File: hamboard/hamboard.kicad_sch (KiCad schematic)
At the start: 38 parts, among them J1 Conn_01x03_Male, J2 Conn_01x24_Male, J3 USB_B_Micro, J4 Screw_Terminal_Btn, J5 Screw_Terminal_01x02, J6 programmer, Q1 AO3400A, Q2 S8050, Q3 S8050, U1 PCA9557PW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

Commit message: board: bom
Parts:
- removed J1: Conn_01x03_Male, Connector_PinHeader_2.54mm:PinHeader_1x03_P2.54mm_Vertical, symbol Connector:Conn_01x03_Male
- removed Q2, Q3: S8050, Package_TO_SOT_THT:TO-92_Inline, symbol Transistor_BJT:S8050
- removed TP1, TP2, TP3: TestPoint, TestPoint:TestPoint_Pad_D1.5mm, symbol Connector:TestPoint
- added C34: 15pF, Capacitor_SMD:C_0805_2012Metric, symbol Device:C
- added J1: i2c, TerminalBlock:TerminalBlock_bornier-4_P5.08mm, symbol Connector:Screw_Terminal_01x04
- added J10: Conn_01x03_Male, Connector_PinHeader_2.54mm:PinHeader_1x03_P2.54mm_Vertical, symbol Connector:Conn_01x03_Male
- added Q2, Q3: S8050, Package_TO_SOT_SMD:SOT-23, symbol Device:Q_NPN_BEC
- added R6: 1k, Resistor_SMD:R_0805_2012Metric, symbol Device:R
- added TP10, TP11: TestPoint, TestPoint:TestPoint_Pad_D1.5mm, symbol Connector:TestPoint
- C1: LCSC (none) -> C282732
- C2: LCSC (none) -> C29277
- C24, C4, C6: value C -> 1uF; LCSC (none) -> C2798196
- C26, C7: value C -> 100nF; LCSC (none) -> C282732
- C27, C8: value C -> 10nF; LCSC (none) -> C376921
- C3: value 0.1uF -> 100nF; LCSC (none) -> C282732
- C5: value ? -> 100nF; LCSC (none) -> C282732
- D1, D2: footprint Diode_SMD:D_SOD-923 -> hamboard:Diodes_DFN1006; LCSC (none) -> C2985641
- J2: footprint (none) -> Connector_FFC-FPC:Hirose_FH12-24S-0.5SH_1x24-1MP_P0.50mm_Horizontal; LCSC (none) -> C2858298
- J3: footprint Connector_USB:USB_Micro-B_Molex-105017-0001 -> Connector_USB:USB_Micro-B_GCT_USB3076-30-A; LCSC (none) -> C132562
- J4, J5: footprint Connector_Phoenix_MSTB:PhoenixContact_MSTBA_2,5_2-G-5,08_1x02_P5.08mm_Horizontal -> TerminalBlock:TerminalBlock_bornier-2_P5.08mm; LCSC (none) -> C394556
- Q1: LCSC (none) -> C347475
- R1, R2, R9: value R -> 10k; LCSC (none) -> C2930231
- R10: LCSC (none) -> C2907288
- R11: value 0R -> 10k; LCSC (none) -> C2930231
- R12, R13, R4, R5, R8: LCSC (none) -> C2930231
- U1: LCSC (none) -> C141380
- U2: LCSC (none) -> C529589
- U3: footprint Package_SO:SOIC-16_3.9x9.9mm_P1.27mm -> Package_SO:SOP-16_3.9x9.9mm_P1.27mm; LCSC (none) -> C84681
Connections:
- net +3V3: now also J1.1 (Pin_1)
- net BTN: now also R6.1; no longer J4.1 (Pin_1)
- net CAM_PCLK: now also C34.1
- net EN: now also Q2.3 (C)
- net GND: now also C34.2, J1.4 (Pin_4)
- net I2C_SCL: now also J1.2 (Pin_2)
- net I2C_SDA: now also J1.3 (Pin_3)
- net IO0: now also Q3.3 (C)
- net at U1.13 (IO6): now also J10.2 (Pin_2)
- net at D2.2 (A2), J3.2 (D-), U3.6 (UD-): now also TP11.1
- net at U1.12 (IO5): now also J10.3 (Pin_3)
- net at U1.14 (IO7): now also J10.1 (Pin_1)
- net at D1.2 (A2), J3.3 (D+), U3.5 (UD+): now also TP10.1
- net at R12.1, U3.13 (~{DTR}): now also Q3.2 (E)
- net at R13.2: now also Q3.1 (B)
- net at R13.1, U3.14 (~{RTS}): now also Q2.2 (E)
- net at R12.2: now also Q2.1 (B)
- new net: J4.1 (Pin_1), R6.2
- no-connect marks 0 -> 10
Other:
- moved on the sheet: C24, C26, C27, C5, C6, C7, C8, J4, R1, R2, R9

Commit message: first pcb layout
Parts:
- J1: footprint TerminalBlock:TerminalBlock_bornier-4_P5.08mm -> Connector_PinHeader_2.54mm:PinHeader_1x04_P2.54mm_Vertical
- U2: footprint lib:XCVR_ESP32-WROVER-E-N4R8 -> XCVR_ESP32-WROVER-E-N4R8; symbol esp32:ESP32-WROVER-E-N4R8 -> hamboard:ESP32-WROVER-E-N4R8
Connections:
- net +24V: now also J5.2 (Pin_2); no longer J5.1 (Pin_1)
- net BTN: now also U2.36 (IO22); no longer U2.6 (IO34)
- net CAM_HREF: now also U2.14 (IO12); no longer U2.24 (IO2)
- net CAM_PCLK: now also U2.9 (IO33); no longer U2.36 (IO22)
- net CAM_PWN: now also U1.6 (IO0); no longer U1.7 (IO1)
- net CAM_RST: now also U1.7 (IO1); no longer U1.6 (IO0)
- net CAM_VSYNC: now also U2.16 (IO13); no longer U2.29 (IO5)
- net CAM_XCLK: now also U2.12 (IO27); no longer U2.30 (IO18)
- net CAM_Y2: now also U2.7 (IO35); no longer U2.10 (IO25)
- net CAM_Y3: now also U2.5 (SENSOR_VN); no longer U2.12 (IO27)
- net CAM_Y4: now also U2.4 (SENSOR_VP); no longer U2.8 (IO32)
- net CAM_Y5: now also U2.6 (IO34); no longer U2.11 (IO26)
- net CAM_Y6: now also U2.8 (IO32); no longer U2.5 (SENSOR_VN)
- net CAM_Y7: now also U2.10 (IO25); no longer U2.4 (SENSOR_VP)
- net CAM_Y8: now also U2.11 (IO26); no longer U2.7 (IO35)
- net CAM_Y9: now also U2.13 (IO14); no longer U2.23 (IO15)
- net GND: now also U2.39_1 (EXP), U2.39_2 (EXP), U2.39_3 (EXP), U2.39_4 (EXP), U2.39_5 (EXP), U2.39_6 (EXP), U2.39_7 (EXP), U2.39_8 (EXP), U2.39_9 (EXP)
- net I2C_SCL: now also U2.23 (IO15); no longer U2.16 (IO13)
- net I2C_SDA: now also U2.24 (IO2); no longer U2.13 (IO14)
- net STEPPER_CS: now also U2.33 (IO21); no longer U2.31 (IO19)
- net STEPPER_DIR: now also U1.14 (IO7); no longer U1.11 (IO4)
- net STEPPER_EN: now also U1.13 (IO6); no longer U1.10 (IO3)
- net STEPPER_SCK: now also U2.31 (IO19); no longer U2.14 (IO12)
- net STEPPER_SDI: now also U2.30 (IO18); no longer U2.26 (IO4)
- net STEPPER_SDO: now also U2.29 (IO5); no longer U2.9 (IO33)
- net STEPPER_STEP: now also U2.26 (IO4); no longer U2.33 (IO21)
- net at Q1.3 (D): now also J5.1 (Pin_1); no longer J5.2 (Pin_2)
- net at J10.3 (Pin_3): now also U1.10 (IO3); no longer U1.12 (IO5)
- net at J10.2 (Pin_2): now also U1.11 (IO4); no longer U1.13 (IO6)
- net at J10.1 (Pin_1): now also U1.12 (IO5); no longer U1.14 (IO7)
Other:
- moved on the sheet: J10

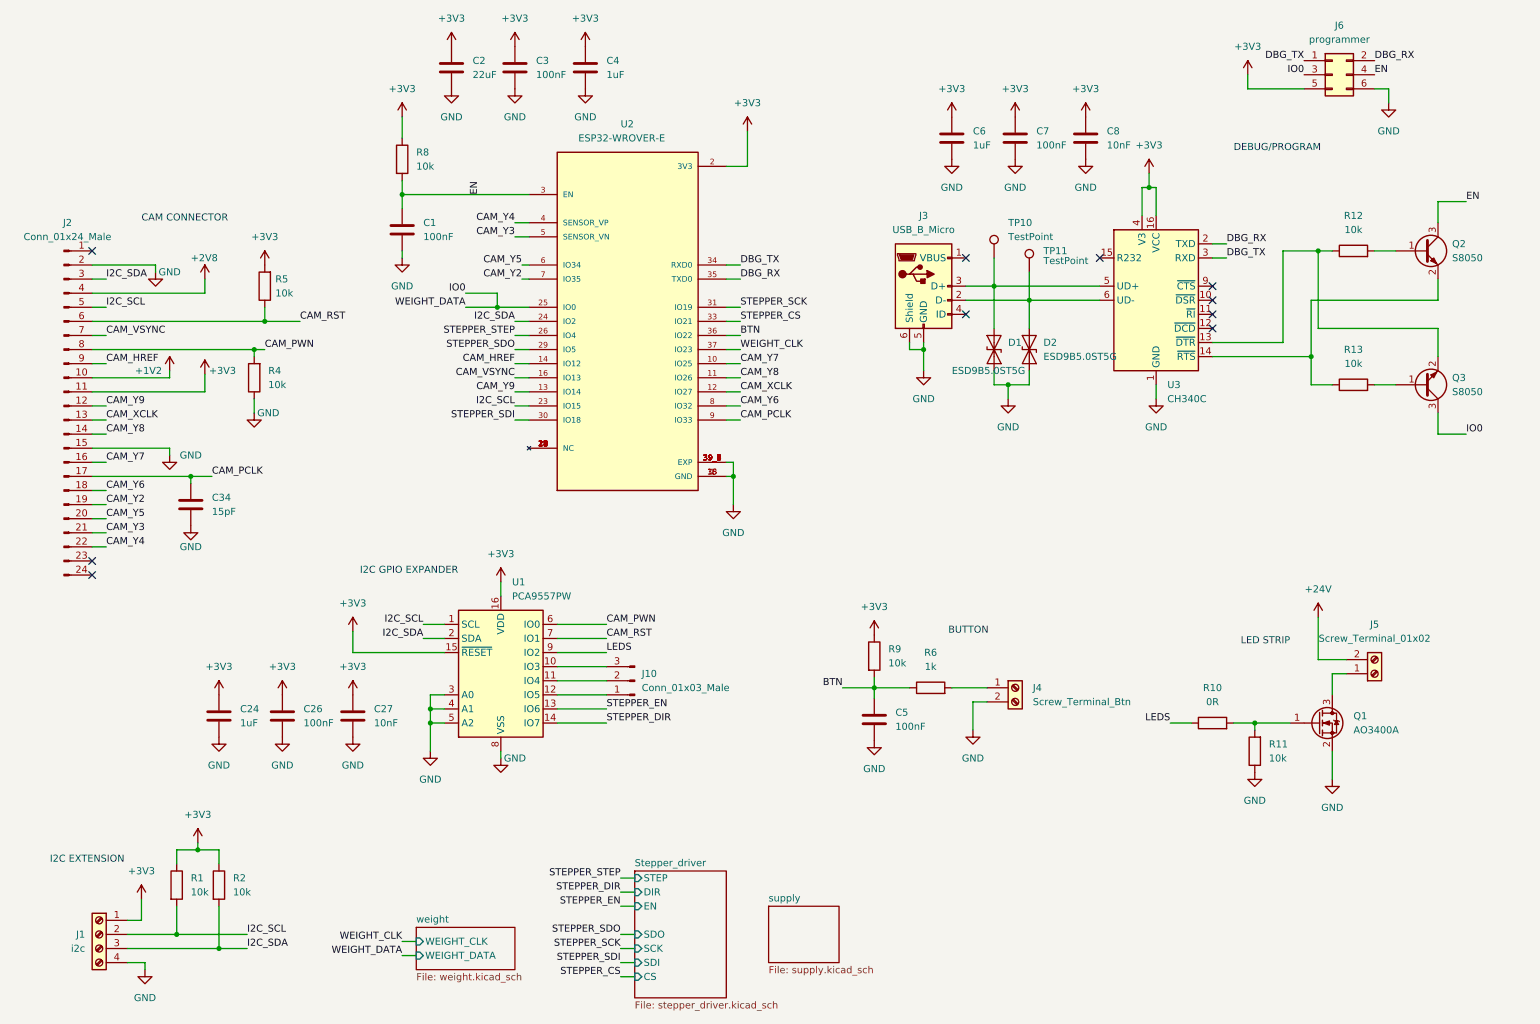
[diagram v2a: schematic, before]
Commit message: pcb: added screws and rerouted everything
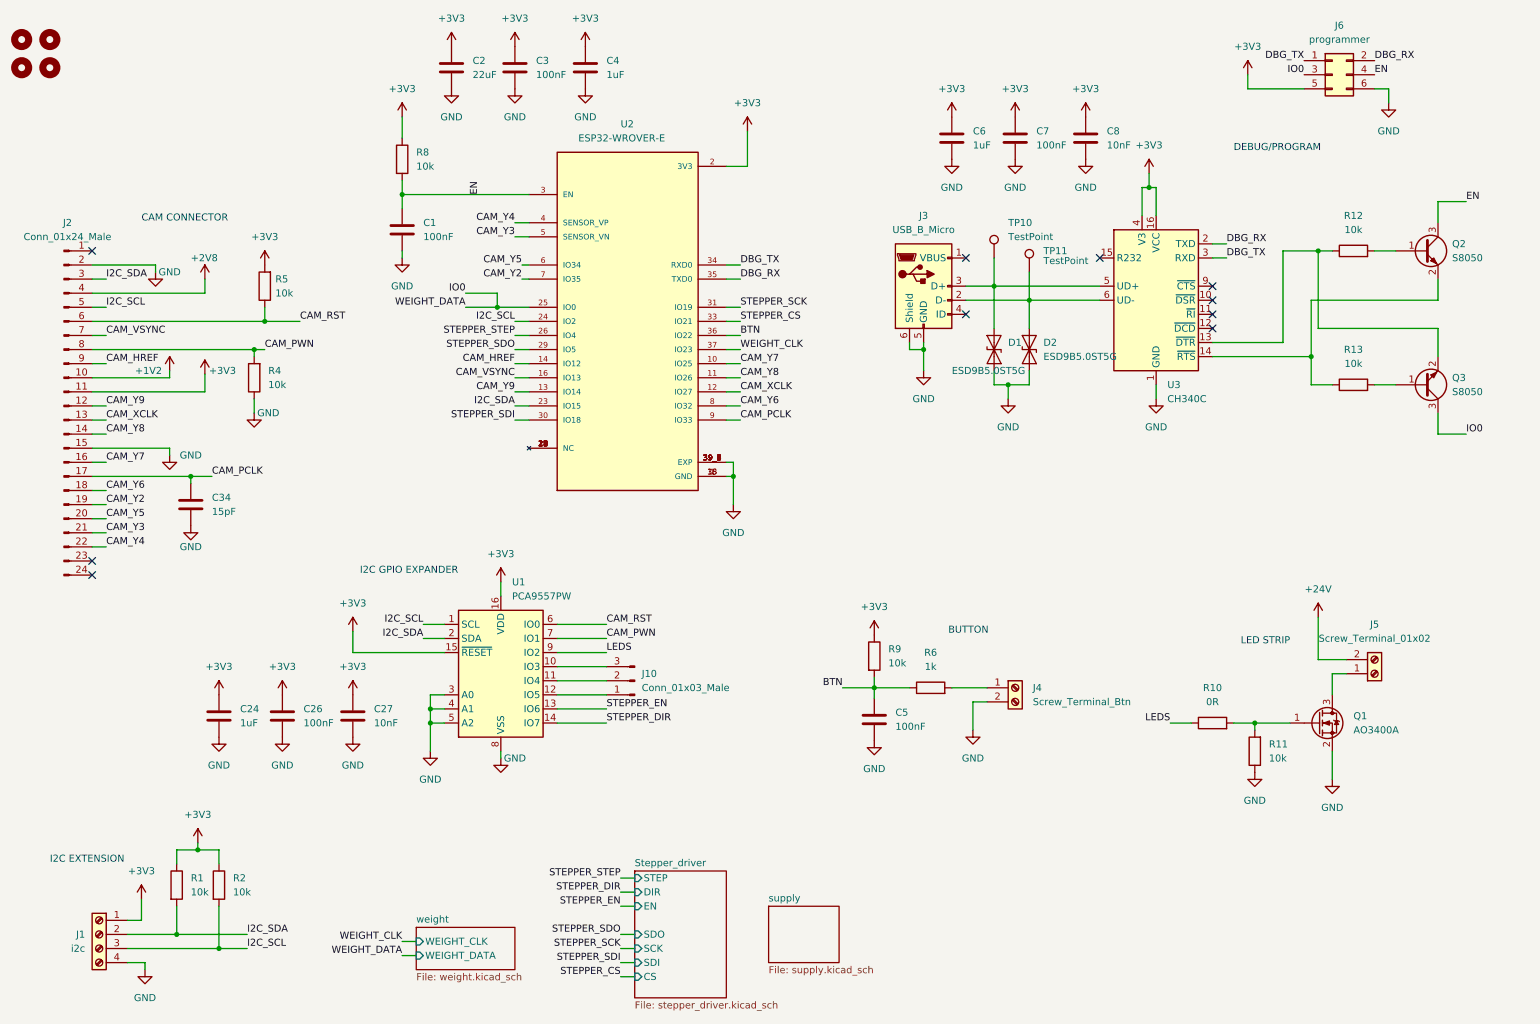
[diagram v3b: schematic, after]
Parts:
- added H1, H2, H3, H4: MountingHole, MountingHole:MountingHole_3.2mm_M3, symbol Mechanical:MountingHole
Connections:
- net CAM_PWN: now also U1.7 (IO1); no longer U1.6 (IO0)
- net CAM_RST: now also U1.6 (IO0); no longer U1.7 (IO1)
- net I2C_SCL: now also J1.3 (Pin_3), R2.2, U2.24 (IO2); no longer J1.2 (Pin_2), R1.2, U2.23 (IO15)
- net I2C_SDA: now also J1.2 (Pin_2), R1.2, U2.23 (IO15); no longer J1.3 (Pin_3), R2.2, U2.24 (IO2)
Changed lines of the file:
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@@
     (effects (font (size 1.27 1.27)) (justify left bottom))
   )
-  (label "I2C_SDA" (at 59.69 181.61 0)
+  (label "I2C_SDA" (at 59.69 179.07 0)
     (effects (font (size 1.27 1.27)) (justify left bottom))
   )
@@
     (effects (font (size 1.27 1.27)) (justify left bottom))
   )
-  (label "I2C_SCL" (at 59.69 179.07 0)
+  (label "I2C_SCL" (at 59.69 181.61 0)
     (effects (font (size 1.27 1.27)) (justify left bottom))
   )
@@
     (effects (font (size 1.27 1.27)) (justify right bottom))
   )
-  (label "I2C_SDA" (at 107.95 68.58 180)
+  (label "I2C_SDA" (at 107.95 83.82 180)
     (effects (font (size 1.27 1.27)) (justify right bottom))
   )
@@
     (effects (font (size 1.27 1.27)) (justify right bottom))
   )
-  (label "CAM_PWN" (at 124.46 123.19 0)
+  (label "CAM_PWN" (at 124.46 125.73 0)
     (effects (font (size 1.27 1.27)) (justify left bottom))
   )
@@
     (effects (font (size 1.27 1.27)) (justify right bottom))
   )
-  (label "I2C_SCL" (at 107.95 83.82 180)
+  (label "I2C_SCL" (at 107.95 68.58 180)
     (effects (font (size 1.27 1.27)) (justify right bottom))
   )
@@
     (effects (font (size 1.27 1.27)) (justify left bottom))
   )
-  (label "CAM_RST" (at 124.46 125.73 0)
+  (label "CAM_RST" (at 124.46 123.19 0)
     (effects (font (size 1.27 1.27)) (justify left bottom))
   )
@@
     (pin "4")
   )
+  (symbol (lib_id "Mechanical:MountingHole") (at 19.05 22.86 0) (unit 1)
+    (in_bom yes) (on_board yes) (fields_autoplaced)
+    (property "Reference" "H2" (id 0) (at 21.59 21.5899 0)
+      (effects (font (size 1.27 1.27)) (justify left) hide)
+    )
+    (property "Value" "MountingHole" (id 1) (at 21.59 24.1299 0)
+      (effects (font (size 1.27 1.27)) (justify left) hide)
+    )
+    (property "Footprint" "MountingHole:MountingHole_3.2mm_M3" (id 2) (at 19.05 22.86 0)
+      (effects (font (size 1.27 1.27)) hide)
+    )
+    (property "Datasheet" "~" (id 3) (at 19.05 22.86 0)
+      (effects (font (size 1.27 1.27)) hide)
+    )
+  )
   (symbol (lib_id "power:+1V2") (at 45.72 77.47 0) (unit 1)
     (in_bom yes) (on_board yes)
@@
     (pin "1")
     (pin "2")
+  )
+  (symbol (lib_id "Mechanical:MountingHole") (at 24.13 17.78 0) (unit 1)
+    (in_bom yes) (on_board yes) (fields_autoplaced)
+    (property "Reference" "H3" (id 0) (at 26.67 16.5099 0)
+      (effects (font (size 1.27 1.27)) (justify left) hide)
+    )
+    (property "Value" "MountingHole" (id 1) (at 26.67 19.0499 0)
+      (effects (font (size 1.27 1.27)) (justify left) hide)
+    )
+    (property "Footprint" "MountingHole:MountingHole_3.2mm_M3" (id 2) (at 24.13 17.78 0)
+      (effects (font (size 1.27 1.27)) hide)
+    )
+    (property "Datasheet" "~" (id 3) (at 24.13 17.78 0)
+      (effects (font (size 1.27 1.27)) hide)
+    )
   )
   (symbol (lib_id "power:+2V8") (at 52.07 60.96 0) (unit 1)
@@
     (pin "1")
     (pin "2")
+  )
+  (symbol (lib_id "Mechanical:MountingHole") (at 19.05 17.78 0) (unit 1)
+    (in_bom yes) (on_board yes) (fields_autoplaced)
+    (property "Reference" "H1" (id 0) (at 21.59 16.5099 0)
+      (effects (font (size 1.27 1.27)) (justify left) hide)
+    )
+    (property "Value" "MountingHole" (id 1) (at 21.59 19.0499 0)
+      (effects (font (size 1.27 1.27)) (justify left) hide)
+    )
+    (property "Footprint" "MountingHole:MountingHole_3.2mm_M3" (id 2) (at 19.05 17.78 0)
+      (effects (font (size 1.27 1.27)) hide)
+    )
+    (property "Datasheet" "~" (id 3) (at 19.05 17.78 0)
+      (effects (font (size 1.27 1.27)) hide)
+    )
   )
   (symbol (lib_id "power:+3V3") (at 50.8 162.56 0) (unit 1)
@@
     (pin "2")
   )
+  (symbol (lib_id "Mechanical:MountingHole") (at 24.13 22.86 0) (unit 1)
+    (in_bom yes) (on_board yes) (fields_autoplaced)
+    (property "Reference" "H4" (id 0) (at 26.67 21.5899 0)
+      (effects (font (size 1.27 1.27)) (justify left) hide)
+    )
+    (property "Value" "MountingHole" (id 1) (at 26.67 24.1299 0)
+      (effects (font (size 1.27 1.27)) (justify left) hide)
+    )
+    (property "Footprint" "MountingHole:MountingHole_3.2mm_M3" (id 2) (at 24.13 22.86 0)
+      (effects (font (size 1.27 1.27)) hide)
+    )
+    (property "Datasheet" "~" (id 3) (at 24.13 22.86 0)
+      (effects (font (size 1.27 1.27)) hide)
+    )
+  )
   (symbol (lib_id "power:GND") (at 78.74 143.51 0) (unit 1)
     (in_bom yes) (on_board yes) (fields_autoplaced)
@@
       (reference "F1") (unit 1) (value "Polyfuse 24V/4A") (footprint "Fuse:Fuse_2920_7451Metric")
     )
+    (path "/7152708c-a746-4345-8572-2a08cbce2cab"
+      (reference "H1") (unit 1) (value "MountingHole") (footprint "MountingHole:MountingHole_3.2mm_M3")
+    )
+    (path "/563ffce6-3179-445e-a692-66231995d1ac"
+      (reference "H2") (unit 1) (value "MountingHole") (footprint "MountingHole:MountingHole_3.2mm_M3")
+    )
+    (path "/5b5dd905-5cf3-4fc8-998a-66cd7dae92f7"
+      (reference "H3") (unit 1) (value "MountingHole") (footprint "MountingHole:MountingHole_3.2mm_M3")
+    )
+    (path "/9879b16b-7ddd-449f-b7b8-508ff38a3ef8"
+      (reference "H4") (unit 1) (value "MountingHole") (footprint "MountingHole:MountingHole_3.2mm_M3")
+    )
     (path "/55b84d23-2619-4bca-a5ce-c99f2a5d964e"
       (reference "J1") (unit 1) (value "i2c") (footprint "Connector_PinHeader_2.54mm:PinHeader_1x04_P2.54mm_Vertical")
@@
       (reference "TP7") (unit 1) (value "TestPoint") (footprint "TestPoint:TestPoint_Pad_D1.5mm")
     )
-    (path "/cf781b29-da03-4e54-8f16-c9e2324f91c7/d88693b6-6dfc-4dd3-877e-759e3c4b167a"
-      (reference "TP8") (unit 1) (value "TestPoint") (footprint "TestPoint:TestPoint_Pad_D1.5mm")
-    )
     (path "/cf781b29-da03-4e54-8f16-c9e2324f91c7/ec254d83-55bb-4786-a17e-eae3949daeeb"

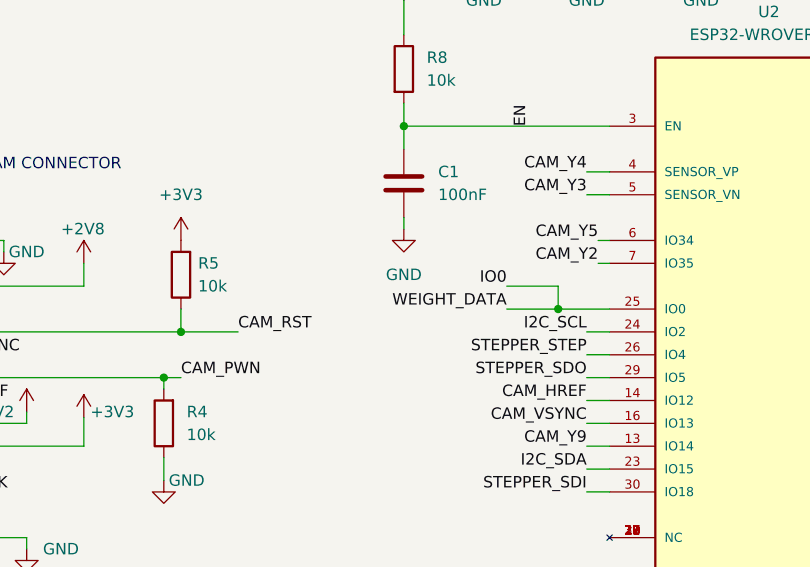
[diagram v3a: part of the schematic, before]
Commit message: board: correct DRC issues
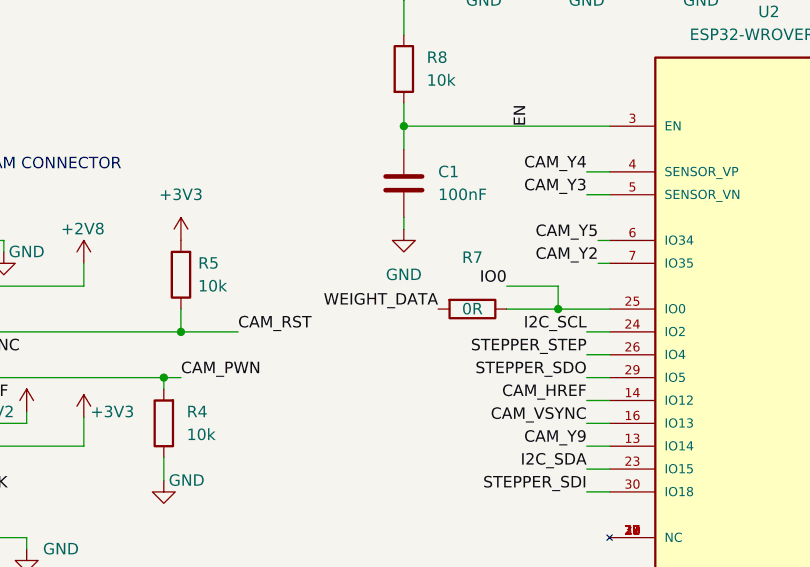
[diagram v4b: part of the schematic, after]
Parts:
- added R7: 0R, Resistor_SMD:R_0805_2012Metric, symbol Device:R
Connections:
- net IO0: now also R7.1
- new net WEIGHT_DATA: R7.2
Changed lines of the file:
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@@
     (effects (font (size 1.27 1.27)) (justify left bottom))
   )
-  (label "WEIGHT_DATA" (at 99.06 66.04 180)
+  (label "WEIGHT_DATA" (at 91.44 66.04 180)
     (effects (font (size 1.27 1.27)) (justify right bottom))
   )
@@
     (pin "8")
     (pin "9")
+  )
+  (symbol (lib_id "Device:R") (at 95.25 66.04 270) (unit 1)
+    (in_bom yes) (on_board yes)
+    (property "Reference" "R7" (id 0) (at 95.25 60.325 90))
+    (property "Value" "0R" (id 1) (at 95.25 66.04 90))
+    (property "Footprint" "Resistor_SMD:R_0805_2012Metric" (id 2) (at 95.25 64.262 90)
+      (effects (font (size 1.27 1.27)) hide)
+    )
+    (property "Datasheet" "~" (id 3) (at 95.25 66.04 0)
+      (effects (font (size 1.27 1.27)) hide)
+    )
+    (property "LCSC" "C2930231" (id 4) (at 93.9799 64.135 0)
+      (effects (font (size 1.27 1.27)) hide)
+    )
+    (pin "1")
+    (pin "2")
   )
   (symbol (lib_id "Device:R") (at 233.68 140.97 90) (unit 1)
@@
       (reference "R6") (unit 1) (value "1k") (footprint "Resistor_SMD:R_0805_2012Metric")
     )
+    (path "/147d7026-5bd9-4756-8c12-bcab3429c469"
+      (reference "R7") (unit 1) (value "0R") (footprint "Resistor_SMD:R_0805_2012Metric")
+    )
     (path "/3db32334-eac2-48ca-a9a6-7574cd038c35"
       (reference "R8") (unit 1) (value "10k") (footprint "Resistor_SMD:R_0805_2012Metric")
@@
       (reference "TP4") (unit 1) (value "TestPoint") (footprint "TestPoint:TestPoint_Pad_D1.5mm")
     )
-    (path "/5327a147-68fc-4492-abf9-1c498ebd9599/deb36bfb-47f4-4298-8b09-1117a2a096bc"
-      (reference "TP5") (unit 1) (value "TestPoint") (footprint "TestPoint:TestPoint_Pad_D1.5mm")
-    )
     (path "/cf781b29-da03-4e54-8f16-c9e2324f91c7/262ef5c4-4cf1-41b2-8ac5-4de463b38dbc"
